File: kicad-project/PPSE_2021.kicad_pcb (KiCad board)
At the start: 2 copper layers, 1 part

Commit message: hw: migrate to kicad 6
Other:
- net class Default removed

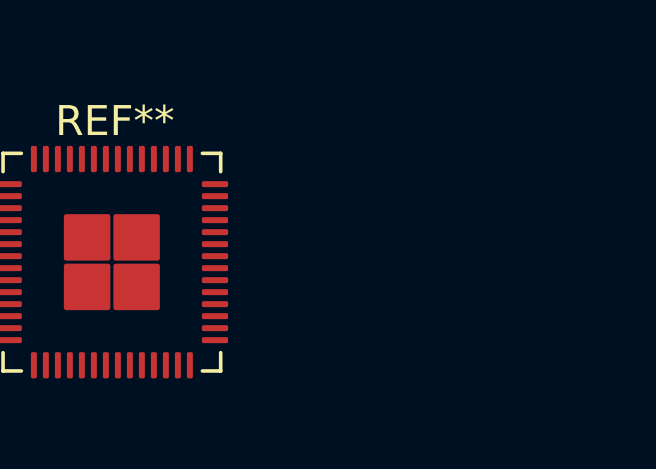
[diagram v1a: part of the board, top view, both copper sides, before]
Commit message: hw: add RP2040 footprint for hand soldering
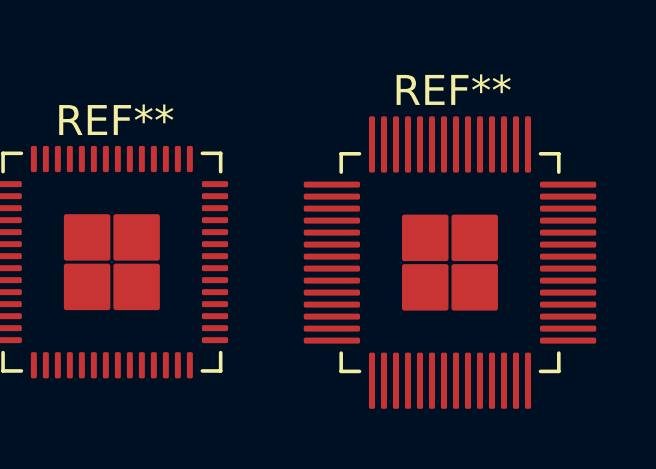
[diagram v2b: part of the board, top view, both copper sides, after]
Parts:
- added REF**: RP2040-Hand-Solder, AA_PPSE_2021:RP2040-Hand-Solder, F.Cu at (110.0, 64.2)
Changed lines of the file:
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@@
     (pad "57" smd roundrect locked (at 0.825 -0.825) (size 1.55 1.55) (layers "F.Cu" "F.Paste" "F.Mask") (roundrect_rratio 0.05))
   )
+  (footprint "AA_PPSE_2021:RP2040-Hand-Solder" (layer "F.Cu")
+    (at 109.95 64.15)
+    (attr through_hole)
+    (fp_text reference "REF**" (at 0.0762 -5.71834) (layer "F.SilkS")
+      (effects (font (size 1 1) (thickness 0.15)))
+    )
+    (fp_text value "RP2040-Hand-Solder" (at 0 5.713219) (layer "F.Fab")
+      (effects (font (size 1 1) (thickness 0.15)))
+    )
+    (fp_line (start 3.627 -3.627) (end 3.01684 -3.627) (layer "F.SilkS") (width 0.12))
+    (fp_line (start 3.627 3.627) (end 3.627 3.01684) (layer "F.SilkS") (width 0.12))
+    (fp_line (start 3.627 -3.01684) (end 3.627 -3.627) (layer "F.SilkS") (width 0.12))
+    (fp_line (start -3.627 3.01684) (end -3.627 3.627) (layer "F.SilkS") (width 0.12))
+    (fp_line (start 3.01684 3.627) (end 3.627 3.627) (layer "F.SilkS") (width 0.12))
+    (fp_line (start -3.627 -3.627) (end -3.627 -3.01684) (layer "F.SilkS") (width 0.12))
+    (fp_line (start -3.627 3.627) (end -3.01684 3.627) (layer "F.SilkS") (width 0.12))
+    (fp_line (start -3.01684 -3.627) (end -3.627 -3.627) (layer "F.SilkS") (width 0.12))
+    (fp_circle (center -4.1148 -3.2004) (end -4.1148 -3.2004) (layer "F.SilkS") (width 0.3) (fill none))
+    (fp_line (start -3.5 -3.5) (end -3.5 3.5) (layer "F.Fab") (width 0.12))
+    (fp_line (start -2.5 -3.5) (end -3.5 -2.5) (layer "F.Fab") (width 0.12))
+    (fp_line (start 3.5 -3.5) (end -3.5 -3.5) (layer "F.Fab") (width 0.12))
+    (fp_line (start 3.5 3.5) (end 3.5 -3.5) (layer "F.Fab") (width 0.12))
+    (fp_line (start -3.5 3.5) (end 3.5 3.5) (layer "F.Fab") (width 0.12))
+    (fp_circle (center -3.2 -3.2) (end -3.2 -3.2) (layer "F.Fab") (width 0.3) (fill none))
+    (pad "1" smd roundrect (at -3.9375 -2.6) (size 1.875 0.2) (layers "F.Cu" "F.Paste" "F.Mask") (roundrect_rratio 0.25))
+    (pad "2" smd roundrect (at -3.9375 -2.2) (size 1.875 0.2) (layers "F.Cu" "F.Paste" "F.Mask") (roundrect_rratio 0.25))
+    (pad "3" smd roundrect (at -3.9375 -1.8) (size 1.875 0.2) (layers "F.Cu" "F.Paste" "F.Mask") (roundrect_rratio 0.25))
+    (pad "4" smd roundrect (at -3.9375 -1.4) (size 1.875 0.2) (layers "F.Cu" "F.Paste" "F.Mask") (roundrect_rratio 0.25))
+    (pad "5" smd roundrect (at -3.9375 -1) (size 1.875 0.2) (layers "F.Cu" "F.Paste" "F.Mask") (roundrect_rratio 0.25))
+    (pad "6" smd roundrect (at -3.9375 -0.6) (size 1.875 0.2) (layers "F.Cu" "F.Paste" "F.Mask") (roundrect_rratio 0.25))
+    (pad "7" smd roundrect (at -3.9375 -0.2) (size 1.875 0.2) (layers "F.Cu" "F.Paste" "F.Mask") (roundrect_rratio 0.25))
+    (pad "8" smd roundrect (at -3.9375 0.2) (size 1.875 0.2) (layers "F.Cu" "F.Paste" "F.Mask") (roundrect_rratio 0.25))
+    (pad "9" smd roundrect (at -3.9375 0.6) (size 1.875 0.2) (layers "F.Cu" "F.Paste" "F.Mask") (roundrect_rratio 0.25))
+    (pad "10" smd roundrect (at -3.9375 1) (size 1.875 0.2) (layers "F.Cu" "F.Paste" "F.Mask") (roundrect_rratio 0.25))
+    (pad "11" smd roundrect (at -3.9375 1.4) (size 1.875 0.2) (layers "F.Cu" "F.Paste" "F.Mask") (roundrect_rratio 0.25))
+    (pad "12" smd roundrect (at -3.9375 1.8) (size 1.875 0.2) (layers "F.Cu" "F.Paste" "F.Mask") (roundrect_rratio 0.25))
+    (pad "13" smd roundrect (at -3.9375 2.2) (size 1.875 0.2) (layers "F.Cu" "F.Paste" "F.Mask") (roundrect_rratio 0.25))
+    (pad "14" smd roundrect (at -3.9375 2.6) (size 1.875 0.2) (layers "F.Cu" "F.Paste" "F.Mask") (roundrect_rratio 0.25))
+    (pad "15" smd roundrect (at -2.6 3.9375 90) (size 1.875 0.2) (layers "F.Cu" "F.Paste" "F.Mask") (roundrect_rratio 0.25))
+    (pad "16" smd roundrect (at -2.2 3.9375 90) (size 1.875 0.2) (layers "F.Cu" "F.Paste" "F.Mask") (roundrect_rratio 0.25))
+    (pad "17" smd roundrect (at -1.8 3.9375 90) (size 1.875 0.2) (layers "F.Cu" "F.Paste" "F.Mask") (roundrect_rratio 0.25))
+    (pad "18" smd roundrect (at -1.4 3.9375 90) (size 1.875 0.2) (layers "F.Cu" "F.Paste" "F.Mask") (roundrect_rratio 0.25))
+    (pad "19" smd roundrect (at -1 3.9375 90) (size 1.875 0.2) (layers "F.Cu" "F.Paste" "F.Mask") (roundrect_rratio 0.25))
+    (pad "20" smd roundrect (at -0.6 3.9375 90) (size 1.875 0.2) (layers "F.Cu" "F.Paste" "F.Mask") (roundrect_rratio 0.25))
+    (pad "21" smd roundrect (at -0.2 3.9375 90) (size 1.875 0.2) (layers "F.Cu" "F.Paste" "F.Mask") (roundrect_rratio 0.25))
+    (pad "22" smd roundrect (at 0.2 3.9375 90) (size 1.875 0.2) (layers "F.Cu" "F.Paste" "F.Mask") (roundrect_rratio 0.25))
+    (pad "23" smd roundrect (at 0.6 3.9375 90) (size 1.875 0.2) (layers "F.Cu" "F.Paste" "F.Mask") (roundrect_rratio 0.25))
+    (pad "24" smd roundrect (at 1 3.9375 90) (size 1.875 0.2) (layers "F.Cu" "F.Paste" "F.Mask") (roundrect_rratio 0.25))
+    (pad "25" smd roundrect (at 1.4 3.9375 90) (size 1.875 0.2) (layers "F.Cu" "F.Paste" "F.Mask") (roundrect_rratio 0.25))
+    (pad "26" smd roundrect (at 1.8 3.9375 90) (size 1.875 0.2) (layers "F.Cu" "F.Paste" "F.Mask") (roundrect_rratio 0.25))
+    (pad "27" smd roundrect (at 2.2 3.9375 90) (size 1.875 0.2) (layers "F.Cu" "F.Paste" "F.Mask") (roundrect_rratio 0.25))
+    (pad "28" smd roundrect (at 2.6 3.9375 90) (size 1.875 0.2) (layers "F.Cu" "F.Paste" "F.Mask") (roundrect_rratio 0.25))
+    (pad "29" smd roundrect (at 3.9375 2.6 180) (size 1.875 0.2) (layers "F.Cu" "F.Paste" "F.Mask") (roundrect_rratio 0.25))
+    (pad "30" smd roundrect (at 3.9375 2.2 180) (size 1.875 0.2) (layers "F.Cu" "F.Paste" "F.Mask") (roundrect_rratio 0.25))
+    (pad "31" smd roundrect (at 3.9375 1.8 180) (size 1.875 0.2) (layers "F.Cu" "F.Paste" "F.Mask") (roundrect_rratio 0.25))
+    (pad "32" smd roundrect (at 3.9375 1.4 180) (size 1.875 0.2) (layers "F.Cu" "F.Paste" "F.Mask") (roundrect_rratio 0.25))
+    (pad "33" smd roundrect (at 3.9375 1 180) (size 1.875 0.2) (layers "F.Cu" "F.Paste" "F.Mask") (roundrect_rratio 0.25))
+    (pad "34" smd roundrect (at 3.9375 0.6 180) (size 1.875 0.2) (layers "F.Cu" "F.Paste" "F.Mask") (roundrect_rratio 0.25))
+    (pad "35" smd roundrect (at 3.9375 0.2 180) (size 1.875 0.2) (layers "F.Cu" "F.Paste" "F.Mask") (roundrect_rratio 0.25))
+    (pad "36" smd roundrect (at 3.9375 -0.2 180) (size 1.875 0.2) (layers "F.Cu" "F.Paste" "F.Mask") (roundrect_rratio 0.25))
+    (pad "37" smd roundrect (at 3.9375 -0.6 180) (size 1.875 0.2) (layers "F.Cu" "F.Paste" "F.Mask") (roundrect_rratio 0.25))
+    (pad "38" smd roundrect (at 3.9375 -1 180) (size 1.875 0.2) (layers "F.Cu" "F.Paste" "F.Mask") (roundrect_rratio 0.25))
+    (pad "39" smd roundrect (at 3.9375 -1.4 180) (size 1.875 0.2) (layers "F.Cu" "F.Paste" "F.Mask") (roundrect_rratio 0.25))
+    (pad "40" smd roundrect (at 3.9375 -1.8 180) (size 1.875 0.2) (layers "F.Cu" "F.Paste" "F.Mask") (roundrect_rratio 0.25))
+    (pad "41" smd roundrect (at 3.9375 -2.2 180) (size 1.875 0.2) (layers "F.Cu" "F.Paste" "F.Mask") (roundrect_rratio 0.25))
+    (pad "42" smd roundrect (at 3.9375 -2.6 180) (size 1.875 0.2) (layers "F.Cu" "F.Paste" "F.Mask") (roundrect_rratio 0.25))
+    (pad "43" smd roundrect (at 2.6 -3.9375 270) (size 1.875 0.2) (layers "F.Cu" "F.Paste" "F.Mask") (roundrect_rratio 0.25))
+    (pad "44" smd roundrect (at 2.2 -3.9375 270) (size 1.875 0.2) (layers "F.Cu" "F.Paste" "F.Mask") (roundrect_rratio 0.25))
+    (pad "45" smd roundrect (at 1.8 -3.9375 270) (size 1.875 0.2) (layers "F.Cu" "F.Paste" "F.Mask") (roundrect_rratio 0.25))
+    (pad "46" smd roundrect (at 1.4 -3.9375 270) (size 1.875 0.2) (layers "F.Cu" "F.Paste" "F.Mask") (roundrect_rratio 0.25))
+    (pad "47" smd roundrect (at 1 -3.9375 270) (size 1.875 0.2) (layers "F.Cu" "F.Paste" "F.Mask") (roundrect_rratio 0.25))
+    (pad "48" smd roundrect (at 0.6 -3.9375 270) (size 1.875 0.2) (layers "F.Cu" "F.Paste" "F.Mask") (roundrect_rratio 0.25))
+    (pad "49" smd roundrect (at 0.2 -3.9375 270) (size 1.875 0.2) (layers "F.Cu" "F.Paste" "F.Mask") (roundrect_rratio 0.25))
+    (pad "50" smd roundrect (at -0.2 -3.9375 270) (size 1.875 0.2) (layers "F.Cu" "F.Paste" "F.Mask") (roundrect_rratio 0.25))
+    (pad "51" smd roundrect (at -0.6 -3.9375 270) (size 1.875 0.2) (layers "F.Cu" "F.Paste" "F.Mask") (roundrect_rratio 0.25))
+    (pad "52" smd roundrect (at -1 -3.9375 270) (size 1.875 0.2) (layers "F.Cu" "F.Paste" "F.Mask") (roundrect_rratio 0.25))
+    (pad "53" smd roundrect (at -1.4 -3.9375 270) (size 1.875 0.2) (layers "F.Cu" "F.Paste" "F.Mask") (roundrect_rratio 0.25))
+    (pad "54" smd roundrect (at -1.8 -3.9375 270) (size 1.875 0.2) (layers "F.Cu" "F.Paste" "F.Mask") (roundrect_rratio 0.25))
+    (pad "55" smd roundrect (at -2.2 -3.9375 270) (size 1.875 0.2) (layers "F.Cu" "F.Paste" "F.Mask") (roundrect_rratio 0.25))
+    (pad "56" smd roundrect (at -2.6 -3.9375 270) (size 1.875 0.2) (layers "F.Cu" "F.Paste" "F.Mask") (roundrect_rratio 0.25))
+    (pad "57" smd roundrect (at 0.825 -0.825) (size 1.55 1.55) (layers "F.Cu" "F.Paste" "F.Mask") (roundrect_rratio 0.05))
+    (pad "57" smd roundrect (at -0.825 0.825) (size 1.55 1.55) (layers "F.Cu" "F.Paste" "F.Mask") (roundrect_rratio 0.05))
+    (pad "57" smd roundrect (at 0.825 0.825) (size 1.55 1.55) (layers "F.Cu" "F.Paste" "F.Mask") (roundrect_rratio 0.05))
+    (pad "57" smd roundrect (at -0.825 -0.825) (size 1.55 1.55) (layers "F.Cu" "F.Paste" "F.Mask") (roundrect_rratio 0.05))
+  )
 )

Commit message: hw: first layout draft
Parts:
- removed REF**: RP2040, footprints:RP2040
- removed REF**: RP2040-Hand-Solder, AA_PPSE_2021:RP2040-Hand-Solder
- added BZ1: Buzzer, Buzzer_Beeper:Buzzer_12x9.5RM7.6, F.Cu at (112.8, 98.8)
- added C1: 18p, Capacitor_SMD:C_0603_1608Metric, F.Cu at (149.5, 100.0)
- added C10: 100n, Capacitor_SMD:C_0603_1608Metric, F.Cu at (136.0, 89.9)
- added C11: 100n, Capacitor_SMD:C_0603_1608Metric, F.Cu at (145.7, 94.9)
- added C12: 100n, Capacitor_SMD:C_0603_1608Metric, F.Cu at (131.1, 97.9)
- added C13: 100n, Capacitor_SMD:C_0603_1608Metric, F.Cu at (139.6, 89.9)
- added C14: 100n, Capacitor_SMD:C_0603_1608Metric, F.Cu at (134.4, 89.9)
- added C15: 100n, Capacitor_SMD:C_0603_1608Metric, F.Cu at (139.5, 103.9)
- added C16: 100n, Capacitor_SMD:C_0603_1608Metric, F.Cu at (131.1, 99.5)
- added C17: 100n, Capacitor_SMD:C_0603_1608Metric, F.Cu at (136.0, 103.9)
- added C18: 10u, Capacitor_SMD:C_0805_2012Metric, F.Cu at (112.1, 122.1)
- added C19: 10u, Capacitor_SMD:C_0805_2012Metric, F.Cu at (114.4, 122.1)
- added C2: 100n, Capacitor_SMD:C_0603_1608Metric, F.Cu at (148.5, 122.9)
- added C20: 100n, Capacitor_SMD:C_0603_1608Metric, F.Cu at (116.5, 122.3)
- added C21: 100n, Capacitor_SMD:C_0603_1608Metric, F.Cu at (128.8, 122.2)
- added C22: 22u, Capacitor_SMD:C_0805_2012Metric, F.Cu at (129.1, 118.4)
- added C23: 22u, Capacitor_SMD:C_0805_2012Metric, F.Cu at (131.5, 118.4)
- added C24: 100n, Capacitor_SMD:C_0603_1608Metric, F.Cu at (172.6, 101.8)
- added C25: 100n, Capacitor_SMD:C_0603_1608Metric, F.Cu at (175.1, 101.8)
- added C3: 18p, Capacitor_SMD:C_0603_1608Metric, F.Cu at (149.5, 94.9)
- added C4: 100n, Capacitor_SMD:C_0603_1608Metric, F.Cu at (137.4, 122.9)
- added C5: DNP 100n, Capacitor_SMD:C_0603_1608Metric, F.Cu at (104.8, 92.8)
- added C6: 100n, Capacitor_SMD:C_0603_1608Metric, F.Cu at (131.1, 101.0)
- added C7: 100n, Capacitor_SMD:C_0603_1608Metric, F.Cu at (145.7, 93.3)
- added C8: 1u, Capacitor_SMD:C_0805_2012Metric, F.Cu at (131.3, 90.8)
- added C9: 1u, Capacitor_SMD:C_0805_2012Metric, F.Cu at (131.3, 92.9)
- added D1: SMAJ15A, Diode_SMD:D_SMA, F.Cu at (95.9, 119.0)
- added D10: CGRA4007, Diode_SMD:D_SMA, F.Cu at (175.9, 117.8)
- added D11: CGRA4007, Diode_SMD:D_SMA, F.Cu at (180.2, 117.8)
- added D12: CGRA4007, Diode_SMD:D_SMA, F.Cu at (184.5, 117.8)
- added D13: CGRA4007, Diode_SMD:D_SMA, F.Cu at (154.4, 117.8)
- added D14: CGRA4007, Diode_SMD:D_SMA, F.Cu at (158.7, 117.8)
- added D15: CGRA4007, Diode_SMD:D_SMA, F.Cu at (162.9, 117.8)
- added D16: CGRA4007, Diode_SMD:D_SMA, F.Cu at (167.2, 117.8)
- added D2: SMAJ15A, Diode_SMD:D_SMA, F.Cu at (127.5, 129.7)
- added D3: SMA S1B, Diode_SMD:D_SMA, F.Cu at (131.4, 129.7)
- added D4: SMA S1B, Diode_SMD:D_SMA, F.Cu at (107.5, 121.0)
- added D5: RBR1VWM30ATFTR, ppse_2021:Package-PMDE, F.Cu at (104.2, 108.7)
- added D6: PWR_LED, LED_SMD:LED_0603_1608Metric, F.Cu at (133.7, 118.6)
- added D7: LED_RGB 5050, LED_SMD:LED_RGB_1210, F.Cu at (113.6, 117.4)
- added D8: D_Zener, Diode_SMD:D_0603_1608Metric, F.Cu at (146.6, 84.3)
- added D9: CGRA4007, Diode_SMD:D_SMA, F.Cu at (171.6, 117.8)
- added F1: 2016L050MR, ppse_2021:2016L Series PPTC, F.Cu at (102.5, 121.1)
- added F2: Fuse 1.5A, ppse_2021:Fuse Holder, F.Cu at (112.9, 129.6)
- added FB1: FerriteBead, Inductor_SMD:L_0603_1608Metric, F.Cu at (100.4, 108.7)
- added H1: MountingHole, MountingHole:MountingHole_3.2mm_M3, F.Cu at (92.7, 46.1)
- added H2: MountingHole, MountingHole:MountingHole_3.2mm_M3, F.Cu at (92.7, 54.1)
- added H3: MountingHole, MountingHole:MountingHole_3.2mm_M3, F.Cu at (84.8, 54.1)
- added H4: MountingHole, MountingHole:MountingHole_3.2mm_M3, F.Cu at (84.8, 46.1)
- added J1: Conn_02x04_Counter_Clockwise, Connector_PinHeader_2.54mm:PinHeader_2x04_P2.54mm_Vertical, F.Cu at (142.6, 109.2)
- added J10: Motor 2, Connector_JST:JST_XH_S5B-XH-A_1x05_P2.50mm_Horizontal, F.Cu at (156.7, 125.2)
- added J2: Conn_02x08_Counter_Clockwise, Connector_PinHeader_2.54mm:PinHeader_2x08_P2.54mm_Vertical, F.Cu at (89.8, 79.8)
- added J3: USB_B_Mini, Connector_USB:USB_Mini-B_Wuerth_65100516121_Horizontal, F.Cu at (94.1, 110.3)
- added J4: 12V IN, Connector_Molex:Molex_Micro-Fit_3.0_43650-0200_1x02_P3.00mm_Horizontal, F.Cu at (97.2, 129.8)
- added J5: Compass, Connector_PinHeader_2.54mm:PinHeader_1x05_P2.54mm_Vertical, F.Cu at (127.2, 77.3)
- added J6: Accelerometer, Connector_PinHeader_2.54mm:PinHeader_1x08_P2.54mm_Vertical, F.Cu at (90.0, 86.6)
- added J7: OLED, Connector_PinHeader_2.54mm:PinHeader_1x04_P2.54mm_Vertical, F.Cu at (113.8, 77.1)
- added J8: Screw_Terminal_01x04, TerminalBlock_TE-Connectivity:TerminalBlock_TE_282834-4_1x04_P2.54mm_Horizontal, F.Cu at (148.8, 78.6)
- added J9: Motor 1, Connector_JST:JST_XH_S5B-XH-A_1x05_P2.50mm_Horizontal, F.Cu at (173.8, 125.2)
- added Q1: 3LP01M, Package_TO_SOT_SMD:SOT-323_SC-70, F.Cu at (169.9, 102.2)
- added Q10: SI2300DS, Package_TO_SOT_SMD:SOT-23, F.Cu at (153.5, 112.1)
- added Q11: SI2300DS, Package_TO_SOT_SMD:SOT-23, F.Cu at (157.7, 112.1)
- added Q12: SI2300DS, Package_TO_SOT_SMD:SOT-23, F.Cu at (162.0, 112.1)
- added Q13: SI2300DS, Package_TO_SOT_SMD:SOT-23, F.Cu at (166.3, 112.1)
- added Q2: PDTC114Y, Package_TO_SOT_SMD:SOT-23, F.Cu at (120.3, 106.6)
- added Q3: BC846A, Package_TO_SOT_SMD:SOT-23, F.Cu at (113.4, 112.2)
- added Q4: BC846A, Package_TO_SOT_SMD:SOT-23, F.Cu at (109.3, 112.2)
- added Q5: BC846A, Package_TO_SOT_SMD:SOT-23, F.Cu at (117.6, 112.2)
- added Q6: SI2300DS, Package_TO_SOT_SMD:SOT-23, F.Cu at (170.6, 112.1)
- added Q7: SI2300DS, Package_TO_SOT_SMD:SOT-23, F.Cu at (174.9, 112.1)
- added Q8: SI2300DS, Package_TO_SOT_SMD:SOT-23, F.Cu at (179.3, 112.1)
- added Q9: SI2300DS, Package_TO_SOT_SMD:SOT-23, F.Cu at (183.6, 112.1)
- added R1: 10k, Resistor_SMD:R_0603_1608Metric, F.Cu at (90.9, 92.9)
- added R10: 33k, Resistor_SMD:R_0603_1608Metric, F.Cu at (123.0, 118.5)
- added R11: 10k, Resistor_SMD:R_0603_1608Metric, F.Cu at (119.3, 118.5)
- added R12: 510, Resistor_SMD:R_0603_1608Metric, F.Cu at (132.3, 115.6)
- added R13: 10k, Resistor_SMD:R_0603_1608Metric, F.Cu at (170.0, 104.9)
- added R14: 4k7, Resistor_SMD:R_0603_1608Metric, F.Cu at (116.4, 106.6)
- added R15: 33k, Resistor_SMD:R_0603_1608Metric, F.Cu at (113.3, 109.6)
- added R16: 470R, Resistor_SMD:R_0603_1608Metric, F.Cu at (113.6, 114.8)
- added R17: 33k, Resistor_SMD:R_0603_1608Metric, F.Cu at (109.2, 109.6)
- added R18: 470R, Resistor_SMD:R_0603_1608Metric, F.Cu at (109.4, 114.8)
- added R19: 33k, Resistor_SMD:R_0603_1608Metric, F.Cu at (117.4, 109.6)
- added R2: 1k, Resistor_SMD:R_0603_1608Metric, F.Cu at (101.0, 92.8)
- added R20: 470R, Resistor_SMD:R_0603_1608Metric, F.Cu at (117.7, 114.8)
- added R21: R_Shunt, Resistor_SMD:R_1210_3225Metric, F.Cu at (155.1, 84.1)
- added R22: R, Resistor_SMD:R_0603_1608Metric, F.Cu at (152.7, 86.8)
- added R23: R, Resistor_SMD:R_0603_1608Metric, F.Cu at (155.8, 86.8)
- added R24: R, Resistor_SMD:R_0603_1608Metric, F.Cu at (149.8, 84.3)
- added R25: R, Resistor_SMD:R_0603_1608Metric, F.Cu at (148.2, 84.3)
- added R26: 22, Resistor_SMD:R_0603_1608Metric, F.Cu at (170.7, 107.7)
- added R27: 22, Resistor_SMD:R_0603_1608Metric, F.Cu at (175.1, 107.6)
- added R28: 22, Resistor_SMD:R_0603_1608Metric, F.Cu at (179.4, 107.7)
- added R29: 22, Resistor_SMD:R_0603_1608Metric, F.Cu at (183.7, 107.7)
- added R3: 10k, Resistor_SMD:R_0603_1608Metric, F.Cu at (145.3, 122.9)
- added R30: 10k, Resistor_SMD:R_0603_1608Metric, F.Cu at (170.7, 109.3)
- added R31: 10k, Resistor_SMD:R_0603_1608Metric, F.Cu at (175.1, 109.3)
- added R32: 10k, Resistor_SMD:R_0603_1608Metric, F.Cu at (179.4, 109.3)
- added R33: 10k, Resistor_SMD:R_0603_1608Metric, F.Cu at (183.7, 109.3)
- added R34: 22, Resistor_SMD:R_0603_1608Metric, F.Cu at (153.7, 107.7)
- added R35: 22, Resistor_SMD:R_0603_1608Metric, F.Cu at (157.9, 107.7)
- added R36: 22, Resistor_SMD:R_0603_1608Metric, F.Cu at (162.1, 107.6)
- added R37: 22, Resistor_SMD:R_0603_1608Metric, F.Cu at (166.4, 107.7)
- added R38: 10k, Resistor_SMD:R_0603_1608Metric, F.Cu at (153.6, 109.3)
- added R39: 10k, Resistor_SMD:R_0603_1608Metric, F.Cu at (157.9, 109.3)
- added R4: 1k, Resistor_SMD:R_0603_1608Metric, F.Cu at (145.8, 96.6)
- added R40: 10k, Resistor_SMD:R_0603_1608Metric, F.Cu at (162.1, 109.3)
- added R41: 10k, Resistor_SMD:R_0603_1608Metric, F.Cu at (166.4, 109.3)
- added R5: DNP 10k, Resistor_SMD:R_0603_1608Metric, F.Cu at (97.9, 92.8)
- added R6: 10k, Resistor_SMD:R_0603_1608Metric, F.Cu at (140.6, 122.9)
- added R7: 27R, Resistor_SMD:R_0603_1608Metric, F.Cu at (131.1, 96.3)
- added R8: 27R, Resistor_SMD:R_0603_1608Metric, F.Cu at (131.1, 94.7)
- added R9: 10k, Resistor_SMD:R_0603_1608Metric, F.Cu at (118.4, 122.3)
- added SRP2512-2R2M1: 2.2u, ppse_2021:Inductor, F.Cu at (126.2, 120.5)
- added SW1: PRG_SW, Button_Switch_SMD:SW_SPST_PTS645, F.Cu at (99.4, 98.8)
- added SW2: RST_SW, Button_Switch_SMD:SW_SPST_PTS645, F.Cu at (92.3, 98.8)
- added SW3: HOME_SW, Button_Switch_SMD:SW_SPST_PTS645, F.Cu at (146.9, 128.8)
- added SW4: EN_SW, Button_Switch_SMD:SW_SPST_PTS645, F.Cu at (138.9, 128.8)
- added TP1: TestPoint, TestPoint:TestPoint_Keystone_5005-5009_Compact, F.Cu at (132.3, 123.4)
- added TP2: TestPoint, TestPoint:TestPoint_Keystone_5005-5009_Compact, F.Cu at (103.0, 113.1)
- added TP3: TestPoint, TestPoint:TestPoint_Keystone_5005-5009_Compact, F.Cu at (125.7, 114.2)
- added TP4: TestPoint, TestPoint:TestPoint_Keystone_5005-5009_Compact, F.Cu at (143.5, 78.0)
- added TP5: TestPoint, TestPoint:TestPoint_Keystone_5005-5009_Compact, F.Cu at (147.4, 89.0)
- added U1: W25Q16JVSS, Package_SO:SOIC-8_5.23x5.23mm_P1.27mm, F.Cu at (105.9, 98.7)
- added U2: RP2040, ppse_2021:RP2040-Hand-Solder, F.Cu at (138.6, 96.8)
- added U3: TPS563201, Package_TO_SOT_SMD:SOT-23-6, F.Cu at (122.3, 121.5)
- added U4: PAM-7Q-0, ppse_2021:PAM-7Q0, F.Cu at (173.7, 87.6)
- added U5: LM2904B, Package_SO:TSSOP-8_4.4x3mm_P0.65mm, F.Cu at (154.3, 89.7)
- added Y1: 12MHz, Crystal:Crystal_SMD_3225-4Pin_3.2x2.5mm, F.Cu at (149.5, 97.5)
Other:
- board outline added: 100 x 60 mm
- board text added: "2 Errors on shunt resistor expected"
- board text added: "Se non c'è spazio, cambiare fusibile"

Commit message: hw: classroom changes
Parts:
- removed SRP2512-2R2M1: 2.2u, ppse_2021:Inductor
- removed U5: LM2904B, Package_SO:TSSOP-8_4.4x3mm_P0.65mm
- added C26: C, Capacitor_SMD:C_0603_1608Metric, F.Cu at (143.0, 86.3)
- added L1: 2.2u, ppse_2021:Inductor, F.Cu at (125.8, 120.4)
- J2: footprint Connector_PinHeader_2.54mm:PinHeader_2x08_P2.54mm_Vertical -> Connector_PinHeader_2.54mm:PinHeader_2x05_P2.54mm_Vertical
- R21: value R_Shunt -> 500m
- moved H1 124.2 mm to (183.7, 130.7)
- moved H2 76.6 mm to (92.2, 130.6)
- moved J2 33.6 mm to (122.9, 85.6)
- moved H3 26.4 mm to (91.8, 79.6)
- moved U1 23.7 mm to (128.1, 107.0), turned to 180 degrees
- moved R23 15.5 mm to (140.3, 85.0), turned to 0 degrees
- moved D1 8.43 mm to (102.5, 113.7), turned to 90 degrees
- moved J4 7.65 mm to (97.2, 122.2)
- moved J9 6.57 mm to (167.2, 125.2)
- moved TP2 5.82 mm to (104.8, 107.5)
- moved J10 5.73 mm to (150.9, 125.2)
- moved D5 4.50 mm to (100.0, 106.9), turned to 0 degrees
- moved C21 3.37 mm to (125.8, 123.7)
- moved C12 3.06 mm to (128.1, 97.9)
- moved C9 3.06 mm to (128.3, 92.9)
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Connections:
- D8 pad 1: /Sensing/Pan_V_Part -> /Control/V_PANEL
- J2 pad 10: /Control/EXT_ADC0 -> /Connectivity/SDA
- J2 pad 2: unconnected-(J2-Pad2) -> /Control/GPIO6
- J2 pad 3: unconnected-(J2-Pad3) -> /Control/GPIO23
- J2 pad 4: unconnected-(J2-Pad4) -> /Control/GPIO24
- J2 pad 5: unconnected-(J2-Pad5) -> /Control/GPIO25
- J2 pad 6: unconnected-(J2-Pad6) -> GND
- J2 pad 7: unconnected-(J2-Pad7) -> /Control/EXT_ADC1
- J2 pad 8: GND -> /Control/EXT_ADC0
- J2 pad 9: /Control/EXT_ADC1 -> /Connectivity/SCL
- R22 pad 2: /Sensing/Shunt_V+ -> /Control/I_PANEL
- R23 pad 1: GND -> /Control/V_PANEL
- R23 pad 2: /Sensing/Shunt_V+ -> GND
- R24 pad 2: /Sensing/Pan_V_Part -> /Control/V_PANEL
- R25 pad 1: /Sensing/Pan_V_Part -> /Control/V_PANEL
- TP5 pad 1: /Sensing/Pan_V_Part -> /Control/V_PANEL
- Y1 pad 3: GND -> /Control/iXOUT
- Y1 pad 4: /Control/iXOUT -> GND
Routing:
- net GND: track 0.00 -> 0.50 mm
